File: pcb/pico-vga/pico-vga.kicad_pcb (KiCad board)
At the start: 4 copper layers, 60.4 x 70.3 mm, 48 parts, among them J1 USB_A, J2 USB_A, J3 USB_A, J4 USB_A, J5 DB15_Female_HighDensity, J6 AudioJack3, J7 Micro_SD_Card_Det, J8 Conn_01x06_Pin, Q1 DMP3099L-7, SW1 SW_Push, U1 Raspberry_Pi_Pico

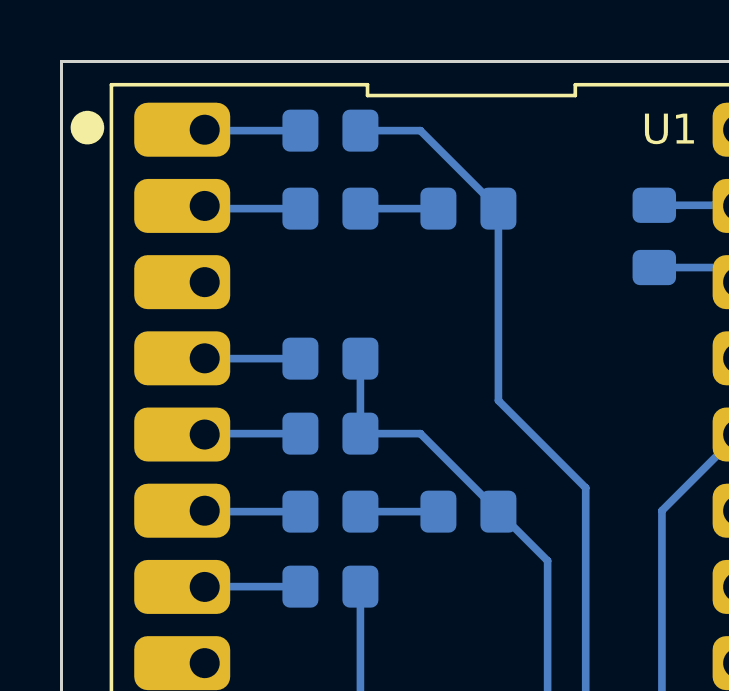
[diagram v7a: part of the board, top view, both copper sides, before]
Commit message: Add JLC tag to pico-vga PCB
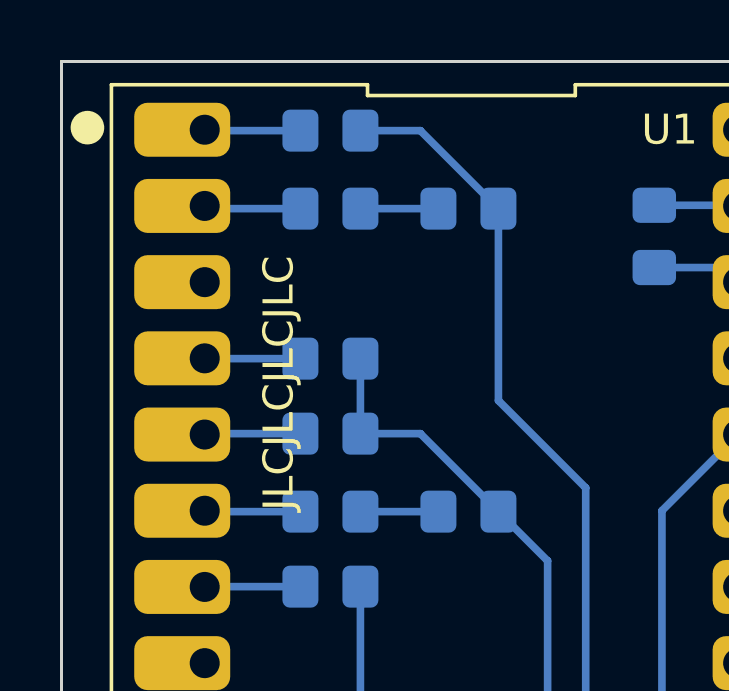
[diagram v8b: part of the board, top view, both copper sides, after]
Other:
- board text added: "JLCJLCJLCJLC"
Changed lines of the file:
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@@
 		(tags "Through hole angled pin header THT 1x06 2.54mm single row")
 		(property "Reference" "J8"
-			(at 9.963 15.24 270)
+			(at 9.963 15.24 -90)
 			(layer "F.SilkS")
 			(effects
@@
 		)
 		(property "Value" "Conn_01x06_Pin"
-			(at 4.385 14.97 270)
+			(at 4.385 14.97 -90)
 			(layer "F.Fab")
 			(effects
@@
 		)
 		(fp_text user "${REFERENCE}"
-			(at 2.77 6.35 360)
+			(at 2.77 6.35 0)
 			(layer "F.Fab")
 			(effects
@@
 		(tags "resistor handsolder")
 		(property "Reference" "R21"
-			(at 0 -1.65 360)
+			(at 0 -1.65 0)
 			(layer "F.SilkS")
 			(effects
@@
 		)
 		(property "Value" "1.8K"
-			(at 0 1.65 360)
+			(at 0 1.65 0)
 			(layer "F.Fab")
 			(effects
@@
 		)
 		(fp_text user "${REFERENCE}"
-			(at 0 0 360)
+			(at 0 0 0)
 			(layer "F.Fab")
 			(effects
@@
 		)
 		(property "Value" "5.1V"
-			(at 0 2.1 360)
+			(at 0 2.1 0)
 			(layer "F.Fab")
 			(effects
@@
 		)
 		(fp_text user "${REFERENCE}"
-			(at 0 -2 360)
+			(at 0 -2 0)
 			(layer "F.Fab")
 			(effects
@@
 		(tags "capacitor handsolder")
 		(property "Reference" "C3"
-			(at 1.016 1.778 360)
+			(at 1.016 1.778 0)
 			(layer "F.SilkS")
 			(effects
@@
 		)
 		(property "Value" "47u"
-			(at 0 1.68 360)
+			(at 0 1.68 0)
 			(layer "F.Fab")
 			(effects
@@
 		)
 		(fp_text user "${REFERENCE}"
-			(at 0 0 360)
+			(at 0 0 0)
 			(layer "F.Fab")
 			(effects
@@
 		(tags "tact sw push 6mm")
 		(property "Reference" "SW1"
-			(at 3.25 2.25 360)
+			(at 3.25 2.25 0)
 			(layer "F.SilkS")
 			(effects
@@
 		)
 		(property "Value" "SW_Push"
-			(at 3.75 6.7 270)
+			(at 3.75 6.7 -90)
 			(layer "F.Fab")
 			(hide yes)
@@
 		)
 		(fp_text user "${REFERENCE}"
-			(at 3.25 2.25 270)
+			(at 3.25 2.25 -90)
 			(layer "F.Fab")
 			(hide yes)
@@
 		(tags "capacitor handsolder")
 		(property "Reference" "C6"
-			(at -2.794 0 270)
+			(at -2.794 0 -90)
 			(layer "F.SilkS")
 			(effects
@@
 		(tags "SOD-123")
 		(property "Reference" "D1"
-			(at 0 0 360)
+			(at 0 0 0)
 			(layer "B.SilkS")
 			(effects
@@
 		)
 		(property "Value" "3.6V"
-			(at 0 -2.1 360)
+			(at 0 -2.1 0)
 			(layer "B.Fab")
 			(effects
@@
 		)
 		(fp_text user "${REFERENCE}"
-			(at 0 2 360)
+			(at 0 2 0)
 			(layer "B.Fab")
 			(effects
@@
 		(tags "capacitor handsolder")
 		(property "Reference" "C4"
-			(at 1.016 1.778 360)
+			(at 1.016 1.778 0)
 			(layer "B.SilkS")
 			(effects
@@
 		)
 		(property "Value" "47u"
-			(at 0 -1.68 360)
+			(at 0 -1.68 0)
 			(layer "B.Fab")
 			(effects
@@
 		)
 		(fp_text user "${REFERENCE}"
-			(at 0 0 360)
+			(at 0 0 0)
 			(layer "B.Fab")
 			(effects
@@
 		(tags "resistor handsolder")
 		(property "Reference" "R3"
-			(at 3.048 0 360)
+			(at 3.048 0 0)
 			(layer "B.SilkS")
 			(effects
@@
 		)
 		(property "Value" "4.7K"
-			(at 0 -1.65 360)
+			(at 0 -1.65 0)
 			(layer "B.Fab")
 			(effects
@@
 		)
 		(fp_text user "${REFERENCE}"
-			(at 0 0 360)
+			(at 0 0 0)
 			(layer "B.Fab")
 			(effects
@@
 		(tags "resistor handsolder")
 		(property "Reference" "R22"
-			(at 0 -1.7 360)
+			(at 0 -1.7 0)
 			(layer "B.SilkS")
 			(effects
@@
 		)
 		(property "Value" "1.8K"
-			(at 0 -1.65 360)
+			(at 0 -1.65 0)
 			(layer "B.Fab")
 			(effects
@@
 		)
 		(fp_text user "${REFERENCE}"
-			(at 0 0 360)
+			(at 0 0 0)
 			(layer "B.Fab")
 			(effects
@@
 		(tags "SOD-123")
 		(property "Reference" "D2"
-			(at 0 0 360)
+			(at 0 0 0)
 			(layer "B.SilkS")
 			(effects
@@
 		)
 		(property "Value" "3.6V"
-			(at 0 -2.1 360)
+			(at 0 -2.1 0)
 			(layer "B.Fab")
 			(effects
@@
 		)
 		(fp_text user "${REFERENCE}"
-			(at 0 2 360)
+			(at 0 2 0)
 			(layer "B.Fab")
 			(effects
@@
 		)
 	)
+	(gr_text "JLCJLCJLCJLC"
+		(at 22.352 27.178 90)
+		(layer "F.SilkS")
+		(effects
+			(font
+				(size 1 1)
+				(thickness 0.15)
+			)
+			(justify left bottom)
+		)
+	)
